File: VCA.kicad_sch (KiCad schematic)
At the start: 28 parts

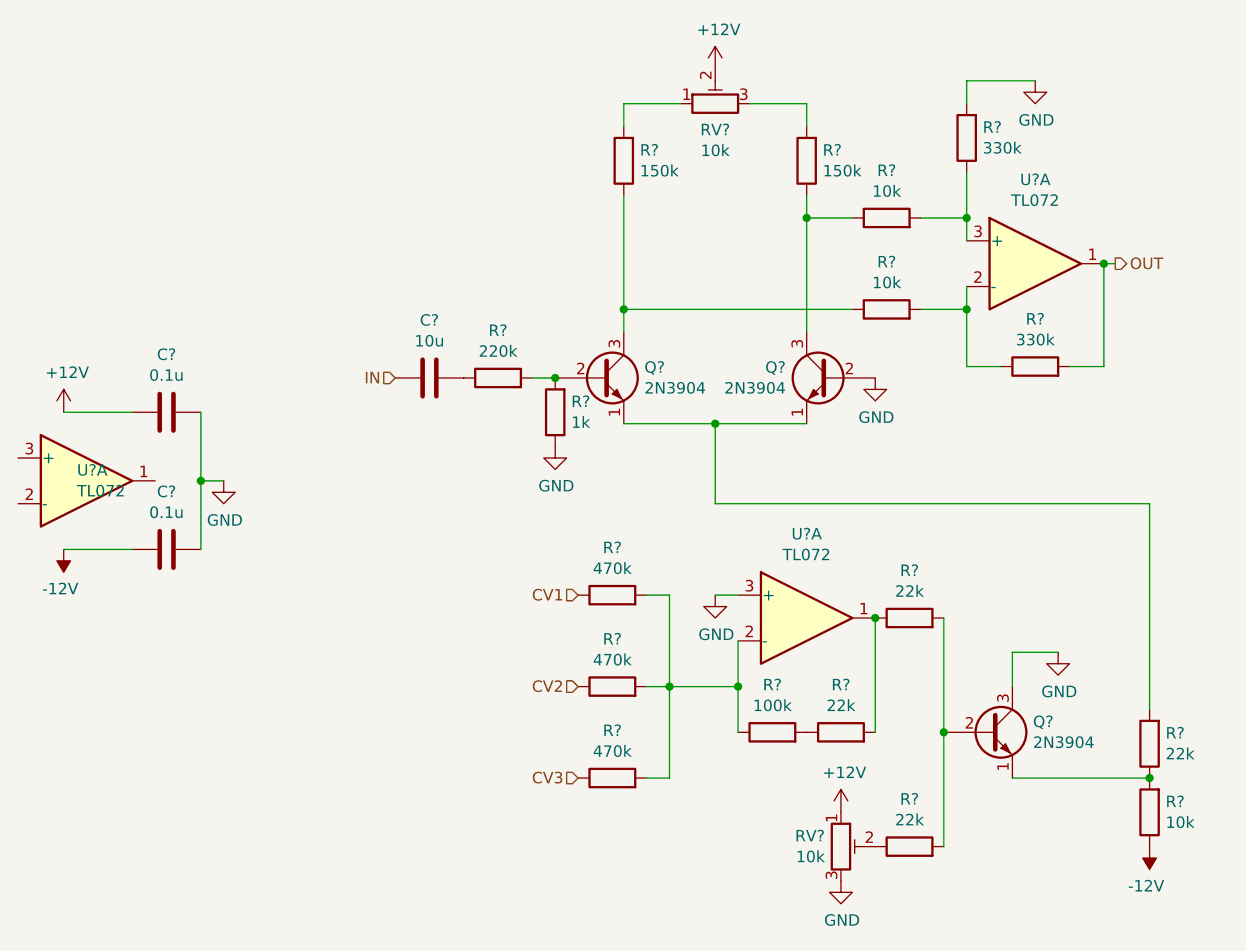
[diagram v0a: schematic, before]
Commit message: Finish schematic
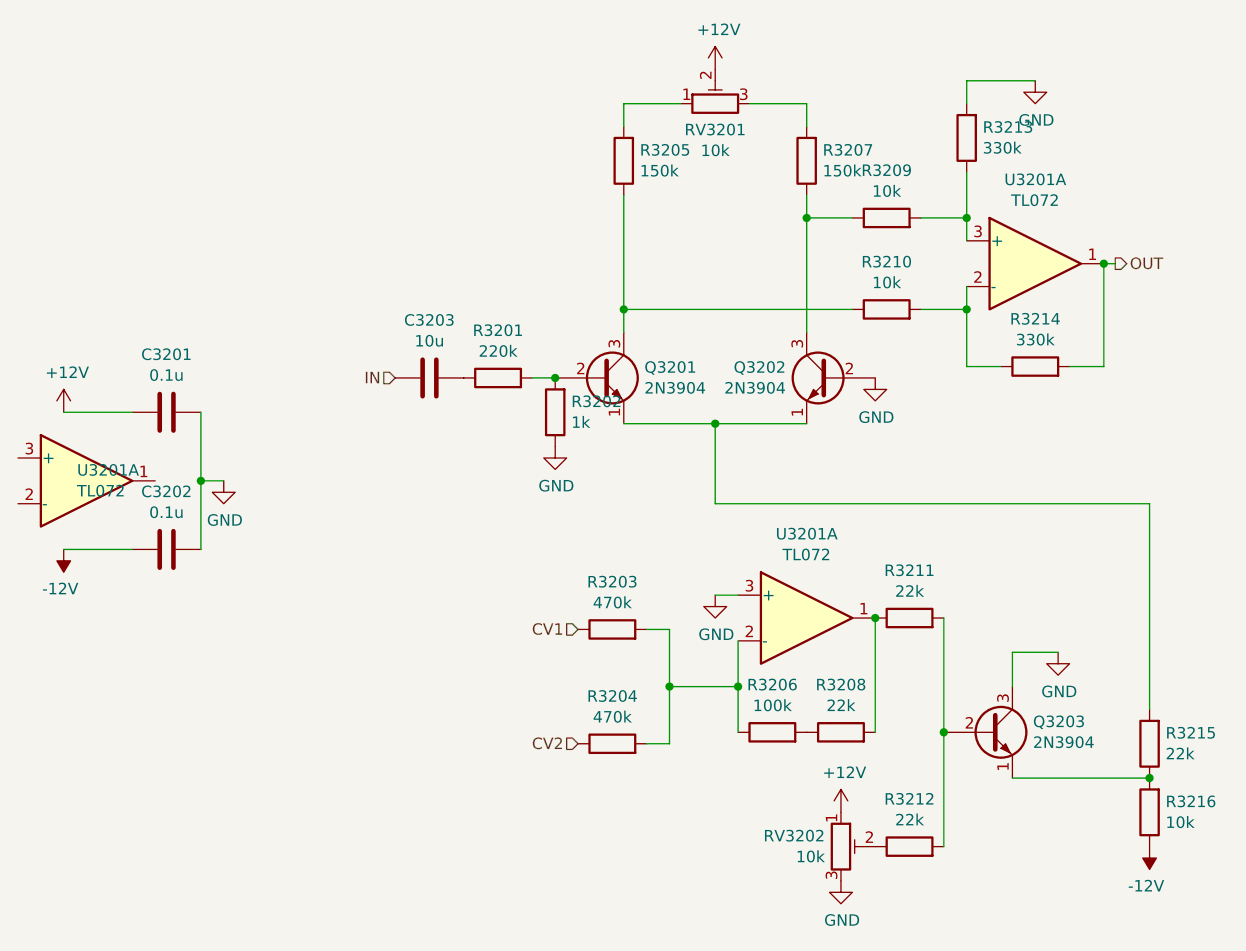
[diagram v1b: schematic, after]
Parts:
- removed R?: 470k, Resistor_THT:R_Axial_DIN0207_L6.3mm_D2.5mm_P7.62mm_Horizontal, symbol Device:R
- Q3201, Q3202, Q3203: renamed from Q?; footprint Package_TO_SOT_THT:TO-92_Inline -> Package_TO_SOT_THT:TO-92_HandSolder
- RV3201, RV3202: renamed from RV?; footprint Potentiometer_THT:Potentiometer_Runtron_RM-065_Vertical -> Custom:Potentiometer_Runtron_RM-065_Vertical_Improved
- gave numbers to parts that had none: 20
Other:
- moved on the sheet: R3203, R3204
